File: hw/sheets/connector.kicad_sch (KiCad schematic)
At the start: 1 part, among them J1 AH58893-T9B10-3F

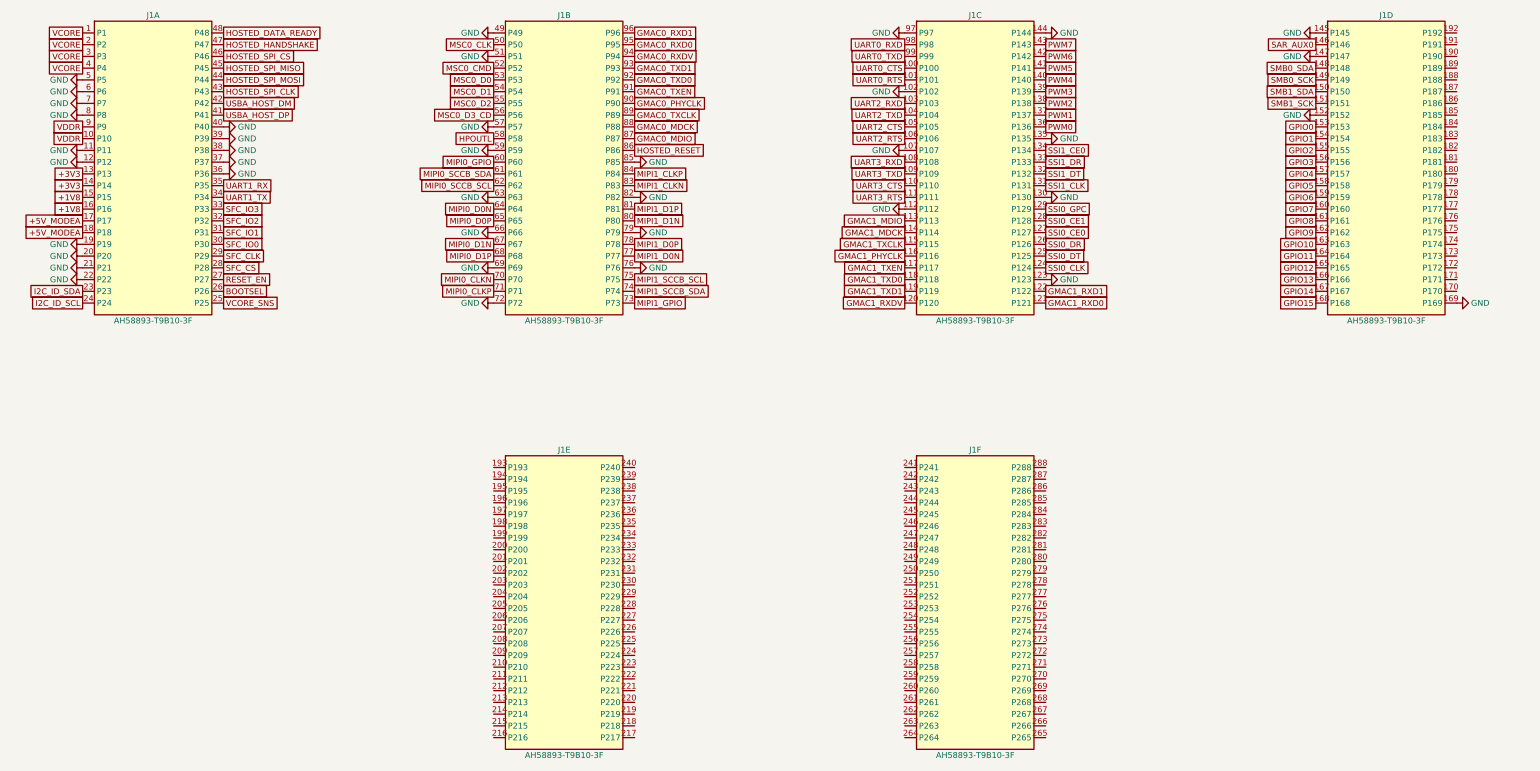
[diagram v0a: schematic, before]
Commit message: Carrier board: break out all remaining J1 pins to spare headers
Per explicit direction: every J1 pin still unused after the SS8
superset breakout (unit 4's 170-192 tail + units 5-6, 119 pins total)
now gets a raw SPARE_P<n> global label (n = the literal connector pin
number) routed to 5 new headers (J31-J35, grouped by connector unit
for traceability). No function is assumed for these -- reserved for
whatever a future interposer or bring-up need wants. Each header's
GND reference pin ties to the common GND net rather than consuming a
J1 position, so it's free against the pin/ground budget; this does
trade away some of SS8's "ground is fill" signal-integrity margin on
this connector for maximum future flexibility, which is the point.

Verified: 0 overlaps, netlist diff shows only the 119 new J1 net
assignments + 5 new header refs added (nothing else moved), ERC total
violation count unchanged (426 before/after -- the pin_not_connected
violations these pins carried became the board's existing pin_to_pin
"unspecified pin type" warning class instead, no new categories).
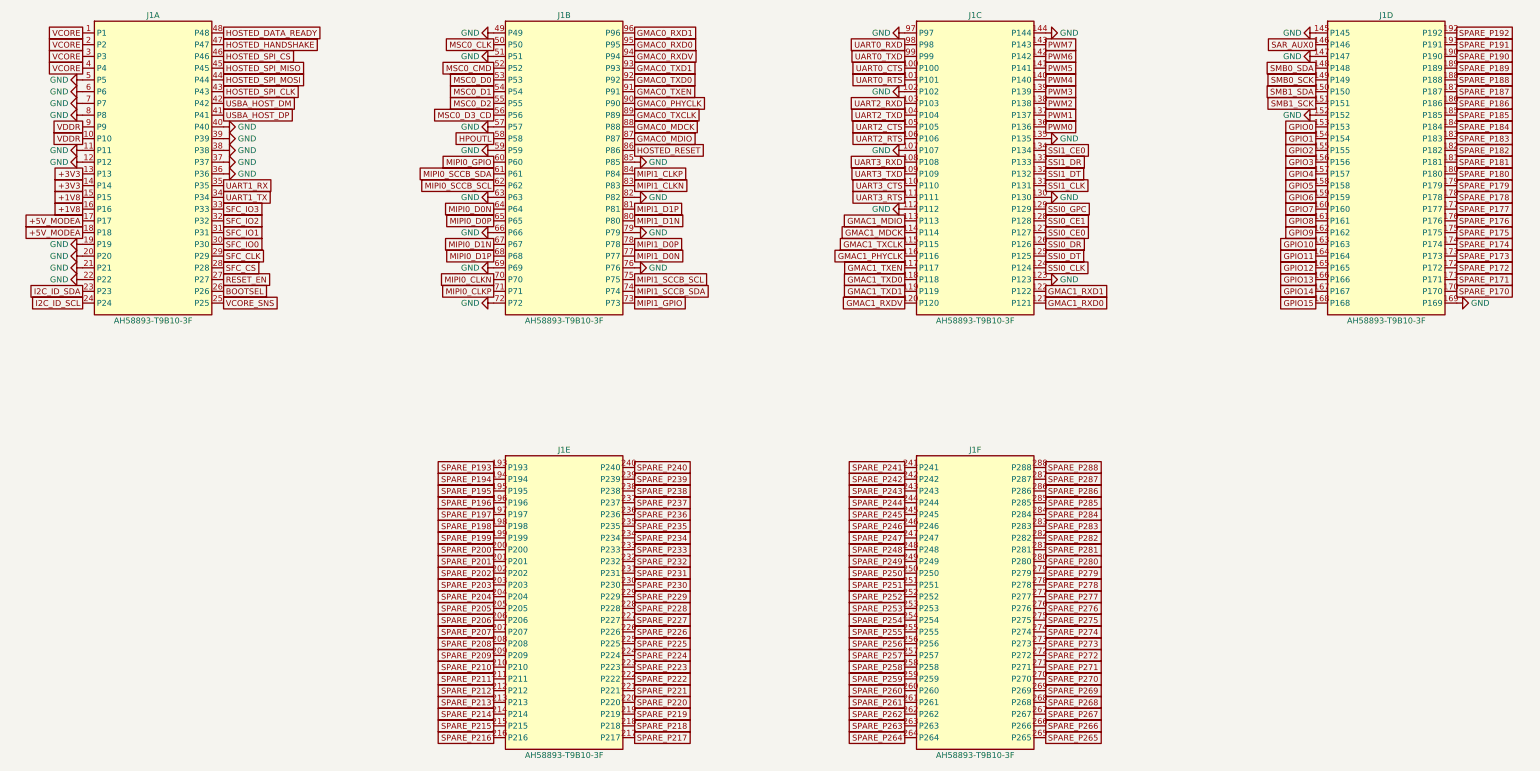
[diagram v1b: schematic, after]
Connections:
- net SPARE_P193: now reaches J1.193 (P193)
- net SPARE_P194: now reaches J1.194 (P194)
- net SPARE_P195: now reaches J1.195 (P195)
- net SPARE_P196: now reaches J1.196 (P196)
- net SPARE_P197: now reaches J1.197 (P197)
- net SPARE_P198: now reaches J1.198 (P198)
- net SPARE_P199: now reaches J1.199 (P199)
- net SPARE_P200: now reaches J1.200 (P200)
- net SPARE_P201: now reaches J1.201 (P201)
- net SPARE_P202: now reaches J1.202 (P202)
- net SPARE_P203: now reaches J1.203 (P203)
- net SPARE_P204: now reaches J1.204 (P204)
- net SPARE_P205: now reaches J1.205 (P205)
- net SPARE_P206: now reaches J1.206 (P206)
- net SPARE_P207: now reaches J1.207 (P207)
- net SPARE_P208: now reaches J1.208 (P208)
- net SPARE_P209: now reaches J1.209 (P209)
- net SPARE_P210: now reaches J1.210 (P210)
- net SPARE_P211: now reaches J1.211 (P211)
- net SPARE_P212: now reaches J1.212 (P212)
- net SPARE_P213: now reaches J1.213 (P213)
- net SPARE_P214: now reaches J1.214 (P214)
- net SPARE_P215: now reaches J1.215 (P215)
- net SPARE_P216: now reaches J1.216 (P216)
- net SPARE_P217: now reaches J1.217 (P217)
- net SPARE_P218: now reaches J1.218 (P218)
- net SPARE_P219: now reaches J1.219 (P219)
- net SPARE_P220: now reaches J1.220 (P220)
- net SPARE_P221: now reaches J1.221 (P221)
- net SPARE_P222: now reaches J1.222 (P222)
- net SPARE_P223: now reaches J1.223 (P223)
- net SPARE_P224: now reaches J1.224 (P224)
- net SPARE_P225: now reaches J1.225 (P225)
- net SPARE_P226: now reaches J1.226 (P226)
- net SPARE_P227: now reaches J1.227 (P227)
- net SPARE_P228: now reaches J1.228 (P228)
- net SPARE_P229: now reaches J1.229 (P229)
- net SPARE_P230: now reaches J1.230 (P230)
- net SPARE_P231: now reaches J1.231 (P231)
- net SPARE_P232: now reaches J1.232 (P232)
- net SPARE_P233: now reaches J1.233 (P233)
- net SPARE_P234: now reaches J1.234 (P234)
- net SPARE_P235: now reaches J1.235 (P235)
- net SPARE_P236: now reaches J1.236 (P236)
- net SPARE_P237: now reaches J1.237 (P237)
- net SPARE_P238: now reaches J1.238 (P238)
- net SPARE_P239: now reaches J1.239 (P239)
- net SPARE_P240: now reaches J1.240 (P240)
- net SPARE_P241: now reaches J1.241 (P241)
- net SPARE_P242: now reaches J1.242 (P242)
- net SPARE_P243: now reaches J1.243 (P243)
- net SPARE_P244: now reaches J1.244 (P244)
- net SPARE_P245: now reaches J1.245 (P245)
- net SPARE_P246: now reaches J1.246 (P246)
- net SPARE_P247: now reaches J1.247 (P247)
- net SPARE_P248: now reaches J1.248 (P248)
- net SPARE_P249: now reaches J1.249 (P249)
- net SPARE_P250: now reaches J1.250 (P250)
- net SPARE_P251: now reaches J1.251 (P251)
- net SPARE_P252: now reaches J1.252 (P252)
- net SPARE_P253: now reaches J1.253 (P253)
- net SPARE_P254: now reaches J1.254 (P254)
- net SPARE_P255: now reaches J1.255 (P255)
- net SPARE_P256: now reaches J1.256 (P256)
- net SPARE_P257: now reaches J1.257 (P257)
- net SPARE_P258: now reaches J1.258 (P258)
- net SPARE_P259: now reaches J1.259 (P259)
- net SPARE_P260: now reaches J1.260 (P260)
- net SPARE_P261: now reaches J1.261 (P261)
- net SPARE_P262: now reaches J1.262 (P262)
- net SPARE_P263: now reaches J1.263 (P263)
- net SPARE_P264: now reaches J1.264 (P264)
- net SPARE_P265: now reaches J1.265 (P265)
- net SPARE_P266: now reaches J1.266 (P266)
- net SPARE_P267: now reaches J1.267 (P267)
- net SPARE_P268: now reaches J1.268 (P268)
- net SPARE_P269: now reaches J1.269 (P269)
- net SPARE_P270: now reaches J1.270 (P270)
- net SPARE_P271: now reaches J1.271 (P271)
- net SPARE_P272: now reaches J1.272 (P272)
- net SPARE_P273: now reaches J1.273 (P273)
- net SPARE_P274: now reaches J1.274 (P274)
- net SPARE_P275: now reaches J1.275 (P275)
- net SPARE_P276: now reaches J1.276 (P276)
- net SPARE_P277: now reaches J1.277 (P277)
- net SPARE_P278: now reaches J1.278 (P278)
- net SPARE_P279: now reaches J1.279 (P279)
- net SPARE_P280: now reaches J1.280 (P280)
- net SPARE_P281: now reaches J1.281 (P281)
- net SPARE_P282: now reaches J1.282 (P282)
- net SPARE_P283: now reaches J1.283 (P283)
- net SPARE_P284: now reaches J1.284 (P284)
- net SPARE_P285: now reaches J1.285 (P285)
- net SPARE_P286: now reaches J1.286 (P286)
- net SPARE_P287: now reaches J1.287 (P287)
- net SPARE_P288: now reaches J1.288 (P288)
- net SPARE_P170: now reaches J1.170 (P170)
- net SPARE_P171: now reaches J1.171 (P171)
- net SPARE_P172: now reaches J1.172 (P172)
- net SPARE_P173: now reaches J1.173 (P173)
- net SPARE_P174: now reaches J1.174 (P174)
- net SPARE_P175: now reaches J1.175 (P175)
- net SPARE_P176: now reaches J1.176 (P176)
- net SPARE_P177: now reaches J1.177 (P177)
- net SPARE_P178: now reaches J1.178 (P178)
- net SPARE_P179: now reaches J1.179 (P179)
- net SPARE_P180: now reaches J1.180 (P180)
- net SPARE_P181: now reaches J1.181 (P181)
- net SPARE_P182: now reaches J1.182 (P182)
- net SPARE_P183: now reaches J1.183 (P183)
- net SPARE_P184: now reaches J1.184 (P184)
- net SPARE_P185: now reaches J1.185 (P185)
- net SPARE_P186: now reaches J1.186 (P186)
- net SPARE_P187: now reaches J1.187 (P187)
- net SPARE_P188: now reaches J1.188 (P188)
- net SPARE_P189: now reaches J1.189 (P189)
- net SPARE_P190: now reaches J1.190 (P190)
- net SPARE_P191: now reaches J1.191 (P191)
- net SPARE_P192: now reaches J1.192 (P192)

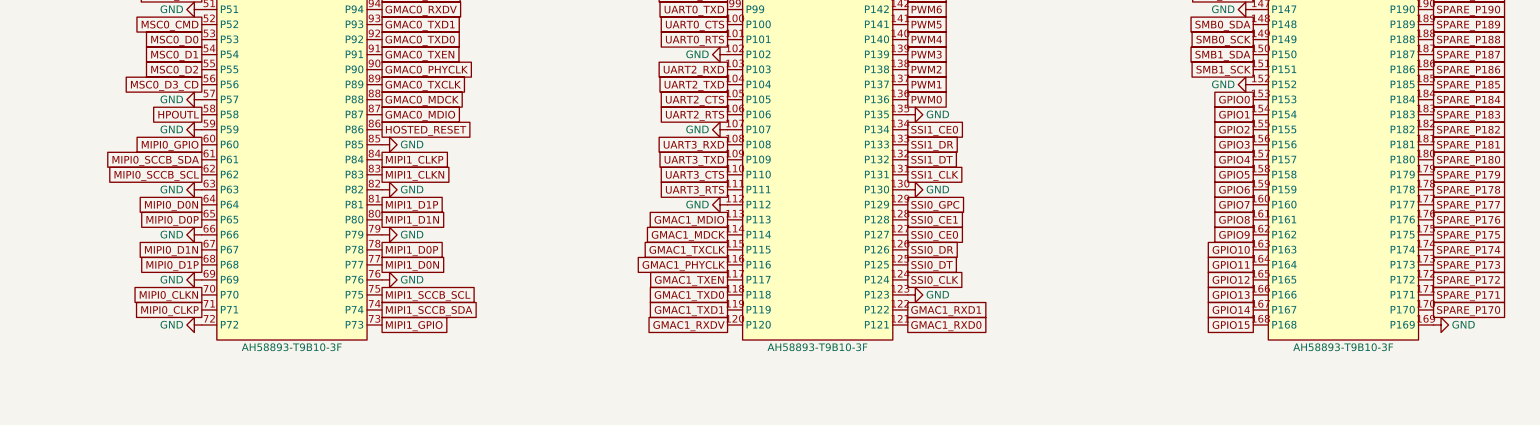
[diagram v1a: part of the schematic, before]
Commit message: Carrier board: audio/FPC pinout fixes matching 3.3, SW2 remap, UART1 breakout, real PCB layout
Schematic fixes (verified pin-for-pin against TeaCup(C)3.3's real netlist,
not assumed):
- J6 audio jack: R1/R2 -> HPOUTL/GND, S -> MICLP, matching 3.3's J10 exactly
  (previous wiring incorrectly tied GND to a schematic pin, G, with no
  matching pad on the real Jack_3.5mm_PJ320D_Horizontal footprint).
- J7/J8 FPC camera connectors: full pin-for-pin remap to match 3.3's real
  J13 pinout -- the previous "standard RPi/Arducam" pinout had power/ground
  swapped, clock/data lanes in the wrong order, and reversed differential
  polarity throughout. Added JP11/JP12 sensor-enable select jumpers
  (GPIO vs hardwired +3V3), replicating 3.3's J15.
- J1 MIPI0/MIPI1 pin order on the connector reordered (CLK/D1/D0, P-before-N)
  to match J7/J8's now-fixed order, so routing between them doesn't need to
  cross over itself.
- HPOUTL relocated from J1 pin 58 (isolated, far from any other audio net)
  down to sit beside MICLP at pins 170-172, geography-first per
  UNIVERSAL.md SS8.
- SW2 (manual power-override switch) throw1/throw4 swapped: throw1 now
  forces ALT, throw4 now forces BMC.
- New J36 header breaks out UART1 (the BMC-ESP32<->J1 console link) for
  external monitoring, same as UART0/2/3 already had.

All verified via isolated before/after ERC diffs -- each change nets to
either 0 or a fully-explained delta against the 429-violation baseline,
never an unexplained regression.

PCB: teacup-carrier.kicad_pcb replaced with the manually-laid-out board
(previously developed as a separate merge-test attempt): real component
placement grouped by circuit block, board outline resized twice to
snugly enclose the layout, GND copper pour on both F.Cu and B.Cu, and
mounting holes repositioned to match. The old rough auto-placed board is
gone.
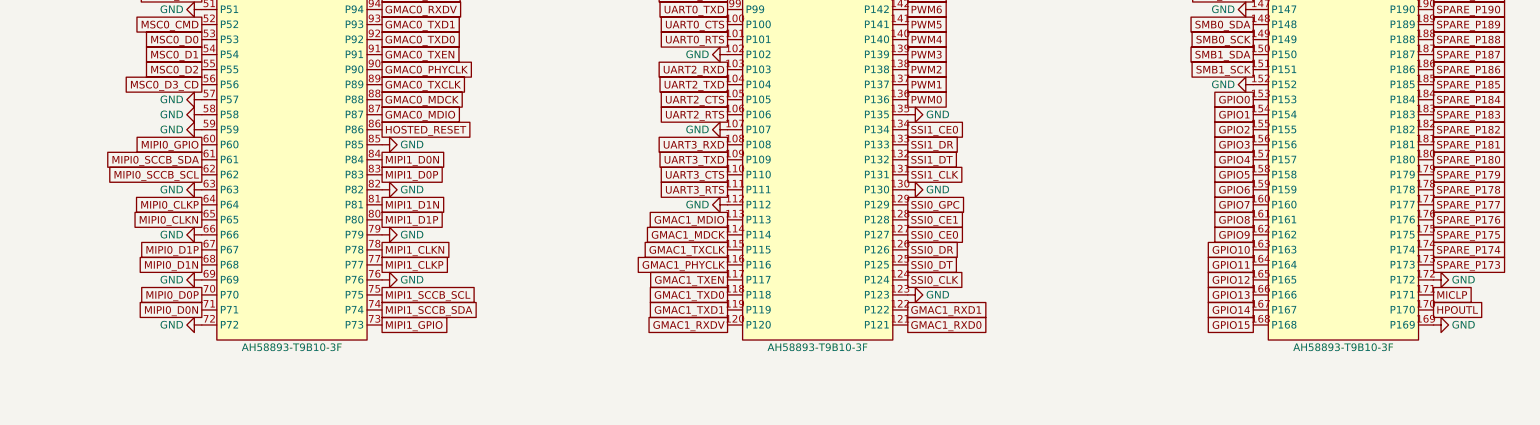
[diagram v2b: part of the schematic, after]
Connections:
- net SPARE_P170 is gone; now on net HPOUTL: J1.170 (P170)
- net SPARE_P172 is gone; now on net GND: J1.172 (P172)
- net GND: now also J1.58 (P58)
- net HPOUTL: no longer J1.58 (P58)
- net MIPI0_CLKN: now also J1.65 (P65); no longer J1.70 (P70)
- net MIPI0_CLKP: now also J1.64 (P64); no longer J1.71 (P71)
- net MIPI0_D0N: now also J1.71 (P71); no longer J1.64 (P64)
- net MIPI0_D0P: now also J1.70 (P70); no longer J1.65 (P65)
- net MIPI0_D1N: now also J1.68 (P68); no longer J1.67 (P67)
- net MIPI0_D1P: now also J1.67 (P67); no longer J1.68 (P68)
- net MIPI1_CLKN: now also J1.78 (P78); no longer J1.83 (P83)
- net MIPI1_CLKP: now also J1.77 (P77); no longer J1.84 (P84)
- net MIPI1_D0N: now also J1.84 (P84); no longer J1.77 (P77)
- net MIPI1_D0P: now also J1.83 (P83); no longer J1.78 (P78)
- net MIPI1_D1N: now also J1.81 (P81); no longer J1.80 (P80)
- net MIPI1_D1P: now also J1.80 (P80); no longer J1.81 (P81)
- net SPARE_P171 renamed MICLP
